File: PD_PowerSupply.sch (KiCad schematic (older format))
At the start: 75 parts, among them J1 2.54mm Header, J2 Screw Terminal, Q1 STL6P3LLH6, Q2 STL6P3LLH6, U1 LM1117LD-3.3, U2 STUSB4500QTR, U3 LMR16006YQ5, U4 LTM8074IY, U5 LTC7106EDDB-1, U6 LMP92064SDE_NOPB, U8 BMD-340-A-R, U9 USB6B1

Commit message: Fixed DRC errors, moved silkscreen
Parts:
- gave numbers to parts that had none: 1
- renumbered TP3 to LED_DATA1
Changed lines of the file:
@@
 Connection ~ 3550 4450
 $Comp
-L Connector:TestPoint TP3
+L Connector:TestPoint LED_DATA1
 U 1 1 5F110793
 P 5650 8850
-F 0 "TP3" H 5600 9100 50  0000 L CNN
+F 0 "LED_DATA1" H 5500 9050 50  0000 L CNN
 F 1 "TestPoint" H 5708 8877 50  0001 L CNN
 F 2 "TestPoint:TestPoint_Pad_D1.0mm" H 5850 8850 50  0001 C CNN
@@
 	8850 1500 12800 1500
 $Comp
-L AQV252GAX:AQV252GAX U?
+L AQV252GAX:AQV252GAX U7
 U 1 1 5F123B82
 P 17100 1950
-F 0 "U?" V 17096 1720 50  0000 R CNN
+F 0 "U7" V 17096 1720 50  0000 R CNN
 F 1 "AQV252GAX" V 17005 1720 50  0000 R CNN
 F 2 "SOP6" H 17100 1950 50  0001 L BNN

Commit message: Setup fab drawing and remove designators from silk
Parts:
- added LMP_CSB1, LTC_CSB1, LTC_EN1, MISO1, MOSI1, SCLK1: TestPoint, TestPoint:TestPoint_Pad_D1.0mm, symbol Connector:TestPoint
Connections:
- net labels added: USB_D_N, USB_D_P, USB_TVS_N, USB_TVS_P
- wire segments 362 -> 373
- no-connect marks 13 -> 14
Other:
- moved on the sheet: C15, C16, C17, C18, D3, I2C_SCL1, I2C_SDA1, L1, R20, R21, R22, U1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

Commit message: Generated gerbers, started BOM setup for PCBWay
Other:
- note added: "FIX INDUCTOR"
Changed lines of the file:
@@
 	1    0    0    -1
 $EndComp
+Text Notes 4800 11550 0    50   ~ 0
+FIX INDUCTOR
 $EndSCHEMATC

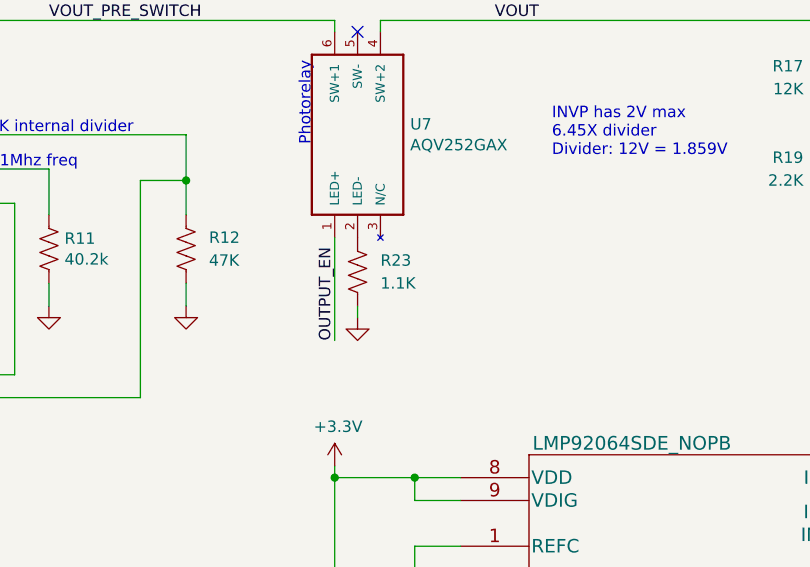
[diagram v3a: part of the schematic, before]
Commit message: Generate gerbers, drill, centroid, and BOM
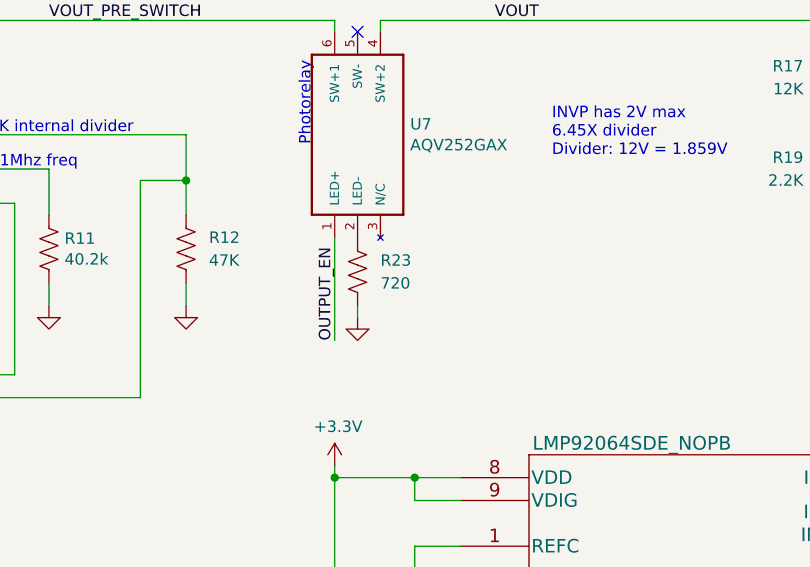
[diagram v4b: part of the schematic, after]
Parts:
- R23: value 1.1K -> 720
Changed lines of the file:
@@
 P 17100 2600
 F 0 "R23" H 17200 2650 50  0000 L CNN
-F 1 "1.1K" H 17200 2550 50  0000 L CNN
+F 1 "720" H 17200 2550 50  0000 L CNN
 F 2 "Resistor_SMD:R_0603_1608Metric" V 17140 2590 50  0001 C CNN
 F 3 "~" H 17100 2600 50  0001 C CNN

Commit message: Switched to PWM DAC
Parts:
- removed U5: LTC7106EDDB-1, ul_LTC7106EDDB:LTC7106EDDB, symbol 2020-04-18_18-56-16:LTC7106EDDB-1
- added BUCK_ENABLE1, DACOUTA1, DACOUTB1: TestPoint, TestPoint:TestPoint_Pad_D1.0mm, symbol Connector:TestPoint
- added C28: 0.1uF, Capacitor_SMD:C_0603_1608Metric, symbol Device:C
- added R24: 10k, Resistor_SMD:R_0603_1608Metric, symbol Device:R_US
- added U5: LTC2644CMS-L10#PBF, SOP65P490X110-12N_LTC2644CMS-L10#PBF, symbol LTC2644CMS-L10_PBF:LTC2644CMS-L10#PBF
- R12: value 47K -> 15k
- R15: value 10k -> DNP
- R7: value 10k -> 3.9k
- renumbered LTC_EN1 to DACPWMA1, LTC_CSB1 to DACPWMB1
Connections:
- net labels added: BUCK_ENABLE, DACPWMA, DACPWMB
- net labels removed: LTC7106_CSB, LTC7106_EN
- wire segments 373 -> 392
- no-connect marks 14 -> 13
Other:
- note added: "Temporarily using STL8P4LLF6\nOriginal PN out of stock"
- note removed: "FIX INDUCTOR"
- note removed: "Switching regulator controller\n(Current DAC)"
- note removed: "VOut accuracy: \n1.0V to 8.9V: 0.06V (nom range)\n9.0V to 12V: 0.25V (high range)"
- moved on the sheet: C10, R10, R15, R7

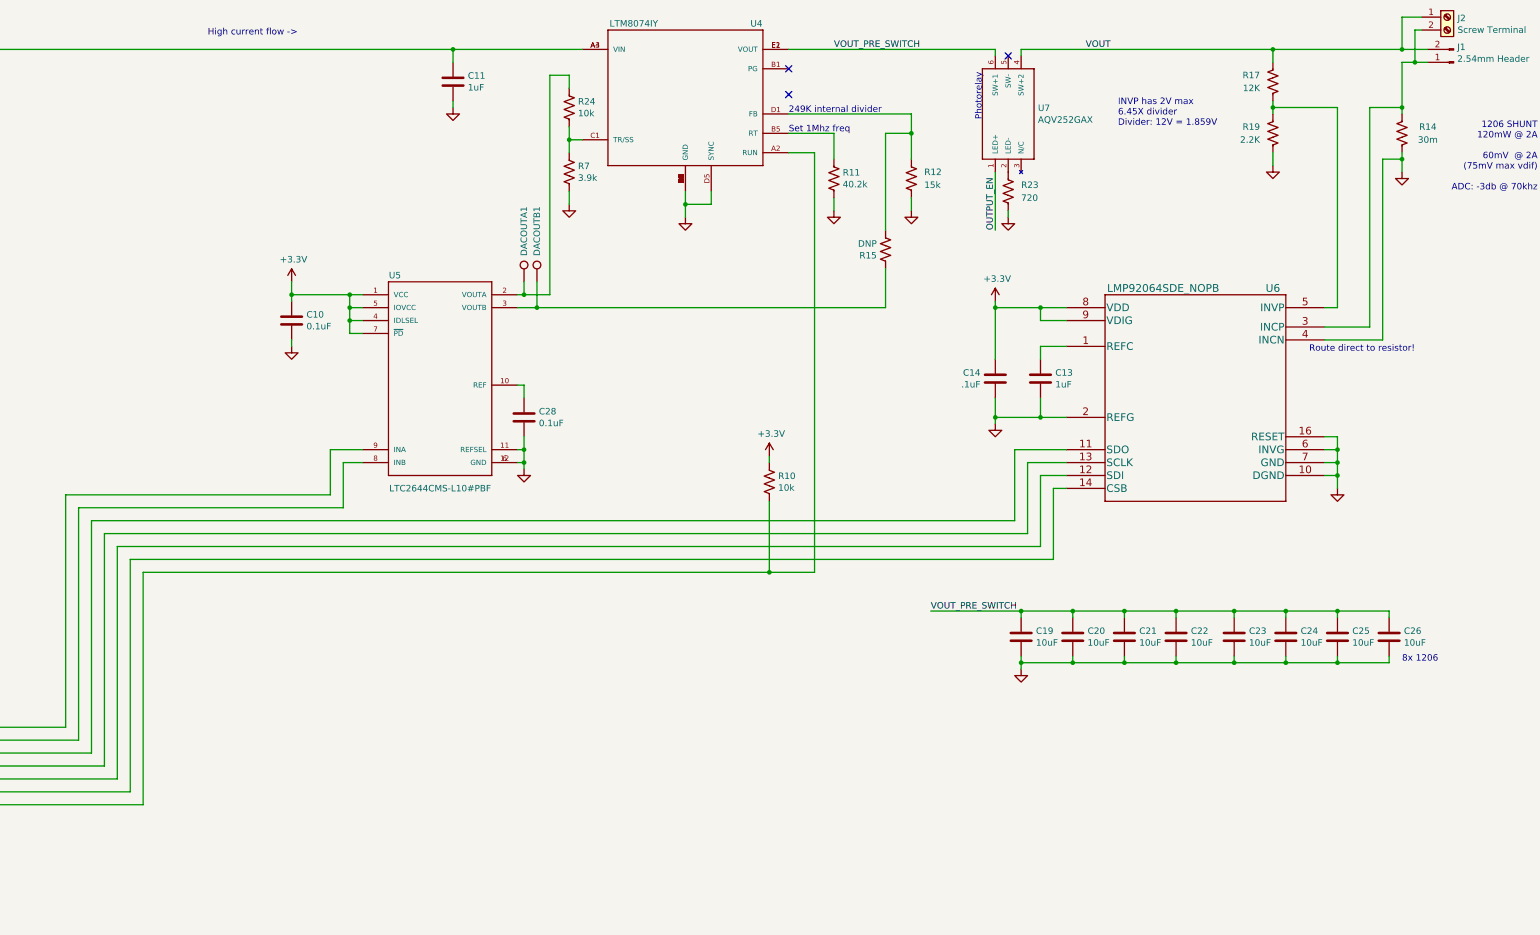
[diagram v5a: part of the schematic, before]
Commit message: Added level shifter for ADC
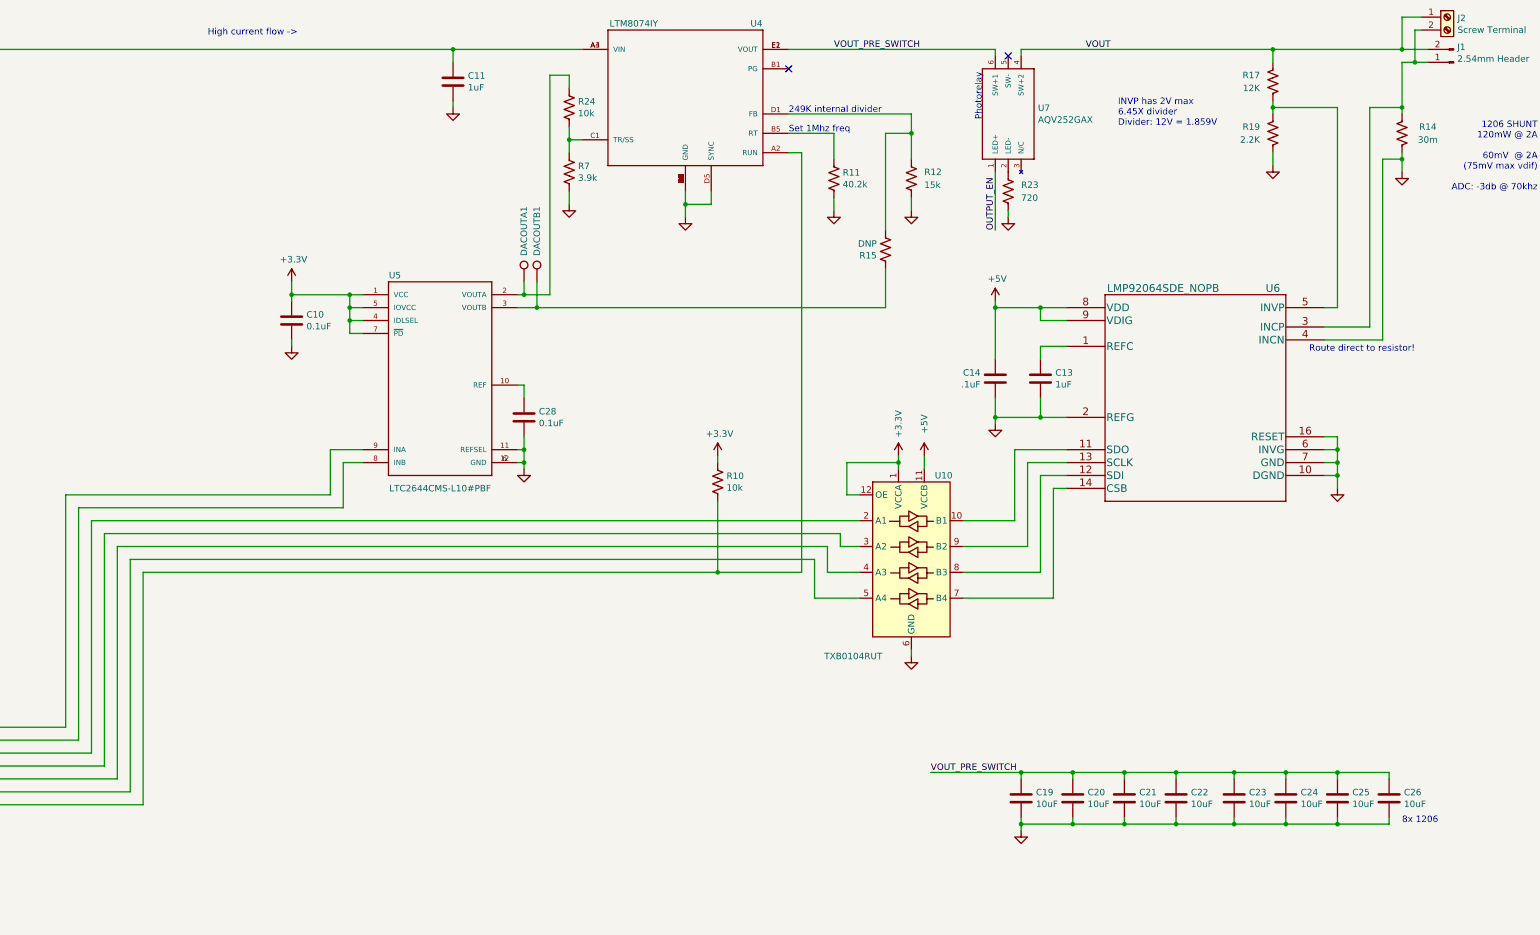
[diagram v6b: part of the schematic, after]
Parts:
- added U10: TXB0104RUT, Package_DFN_QFN:Texas_R_PUQFN-N12, symbol Logic_LevelTranslator:TXB0104RUT
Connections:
- net +3V3: now also U10.1 (VCCA), U10.12 (OE); no longer C14.1, U6.8 (VDD), U6.9 (VDIG)
- net +5V: now also C14.1, U6.8 (VDD), U6.9 (VDIG), U10.11 (VCCB)
- net GND: now also U10.6 (GND)
- net LMP92064_CSB: now also U10.5 (A4); no longer U6.14 (CSB)
- net MISO: now also U10.2 (A1); no longer U6.11 (SDO)
- net MOSI: now also U10.4 (A3); no longer U6.12 (SDI)
- net SCLK: now also U10.3 (A2); no longer U6.13 (SCLK)
- new net: U10.10 (B1), U6.11 (SDO)
- new net: U10.8 (B3), U6.12 (SDI)
- new net: U10.9 (B2), U6.13 (SCLK)
- new net: U10.7 (B4), U6.14 (CSB)
- no-connect marks 13 -> 12
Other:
- moved on the sheet: C19, C20, C21, C22, C23, C24, C25, C26, R10

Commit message: after testing, removed FB resistors and backup PWM DAC channel
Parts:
- removed DACOUTB1: TestPoint, TestPoint:TestPoint_Pad_D1.0mm, symbol Connector:TestPoint
- removed R15: DNP, Resistor_SMD:R_0603_1608Metric, symbol Device:R_US
- removed R21: 54.9K, Resistor_SMD:R_0603_1608Metric, symbol Device:R_US
- removed R22: 10K, Resistor_SMD:R_0603_1608Metric, symbol Device:R_US
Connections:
- net +5V: now also U3.3 (FB)
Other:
- note added: "Internal feedback divider for 5V"
- note added: "USB-C"
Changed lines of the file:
@@
 Title "USB PD Power Supply"
 Date "2020-03-22"
-Rev "1"
-Comp ""
+Rev "2"
+Comp "Captio Labs"
 Comment1 ""
 Comment2 ""
@@
 Wire Wire Line
 	9800 6750 6150 6750
-$Comp
-L Device:R_US R15
-U 1 1 5EAE45A7
-P 16150 3050
-F 0 "R15" H 16218 3096 50  0000 L CNN
-F 1 "DNP" H 16218 3005 50  0000 L CNN
-F 2 "Resistor_SMD:R_0603_1608Metric" V 16190 3040 50  0001 C CNN
-F 3 "~" H 16150 3050 50  0001 C CNN
-	1    16150 3050
-	-1   0    0    1
-$EndComp
 $Comp
 L 2020-05-08_21-34-57:LMP92064SDE_NOPB U6
@@
 Wire Wire Line
 	3600 12700 3600 12650
-$Comp
-L Device:R_US R21
-U 1 1 5F469F42
-P 5700 12250
-F 0 "R21" H 5768 12296 50  0000 L CNN
-F 1 "54.9K" H 5768 12205 50  0000 L CNN
-F 2 "Resistor_SMD:R_0603_1608Metric" V 5740 12240 50  0001 C CNN
-F 3 "~" H 5700 12250 50  0001 C CNN
-	1    5700 12250
-	1    0    0    -1
-$EndComp
 Wire Wire Line
 	5550 11650 5700 11650
-$Comp
-L Device:R_US R22
-U 1 1 5F46B0E3
-P 5700 12650
-F 0 "R22" H 5768 12696 50  0000 L CNN
-F 1 "10K" H 5768 12605 50  0000 L CNN
-F 2 "Resistor_SMD:R_0603_1608Metric" V 5740 12640 50  0001 C CNN
-F 3 "~" H 5700 12650 50  0001 C CNN
-	1    5700 12650
-	1    0    0    -1
-$EndComp
-Wire Wire Line
-	5700 12500 5700 12450
-$Comp
-L power:GND #PWR016
-U 1 1 5F4C1D2E
-P 5700 12850
-F 0 "#PWR016" H 5700 12600 50  0001 C CNN
-F 1 "GND" H 5700 12700 50  0001 C CNN
-F 2 "" H 5700 12850 50  0001 C CNN
-F 3 "" H 5700 12850 50  0001 C CNN
-	1    5700 12850
-	1    0    0    -1
-$EndComp
-Wire Wire Line
-	5700 12850 5700 12800
 $Comp
 L Device:C C17
@@
 Wire Wire Line
 	10300 5450 10300 7250
-Wire Wire Line
-	5700 12450 5700 12400
-Connection ~ 5700 12450
-Wire Wire Line
-	5700 11650 5700 12100
 Text Notes 15400 2000 0    50   ~ 0
 249K internal divider
@@
 Text Notes 7150 1150 0    50   ~ 0
 Temporarily using STL8P4LLF6\nOriginal PN out of stock
-Wire Wire Line
-	16350 2000 16350 2150
-Wire Wire Line
-	16150 2900 16150 2150
-Wire Wire Line
-	16150 2150 16350 2150
-Connection ~ 16350 2150
-Wire Wire Line
-	16350 2150 16350 2350
-Wire Wire Line
-	16150 3500 16150 3200
 $Comp
 L LTC2644CMS-L10_PBF:LTC2644CMS-L10#PBF U5
@@
 	9900 5050 11950 5050
 Wire Wire Line
-	13300 3500 13450 3500
-Wire Wire Line
 	13300 3400 13350 3400
 Text Label 5000 7350 0    50   ~ 0
@@
 	1    0    0    -1
 $EndComp
-$Comp
-L Connector:TestPoint DACOUTB1
-U 1 1 5F3B380F
-P 13450 3300
-F 0 "DACOUTB1" V 13450 3500 50  0000 L CNN
-F 1 "TestPoint" H 13508 3327 50  0001 L CNN
-F 2 "TestPoint:TestPoint_Pad_D1.0mm" H 13650 3300 50  0001 C CNN
-F 3 "~" H 13650 3300 50  0001 C CNN
-	1    13450 3300
-	1    0    0    -1
-$EndComp
 Wire Wire Line
 	13350 3300 13350 3400
-Wire Wire Line
-	13450 3300 13450 3500
-Connection ~ 13450 3500
-Wire Wire Line
-	13450 3500 16150 3500
 Wire Wire Line
 	9800 4950 11850 4950
@@
 Wire Wire Line
 	15500 2300 15500 5550
+Wire Wire Line
+	5700 11650 5700 12450
+Text Notes 4200 12650 0    50   ~ 0
+Internal feedback divider for 5V
+Text Notes 1600 4600 0    50   ~ 0
+USB-C
+Wire Wire Line
+	16350 2000 16350 2350
 $EndSCHEMATC

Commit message: remove feedback divider from 5V buck (internal divider)
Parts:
- U3: symbol Regulator_Switching:LMR16006YQ5 -> PD_PowerSupply-rescue:LMR16006YQ5-Regulator_Switching
- U9: symbol Power_Protection:USB6B1 -> PD_PowerSupply-rescue:USB6B1-Power_Protection
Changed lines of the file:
@@
 	20150 1500 20350 1500
 $Comp
-L Regulator_Switching:LMR16006YQ5 U3
+L PD_PowerSupply-rescue:LMR16006YQ5-Regulator_Switching U3
 U 1 1 5EA28B43
 P 3600 11700
@@
 	2100 3550 2100 3600
 $Comp
-L Power_Protection:USB6B1 U9
+L PD_PowerSupply-rescue:USB6B1-Power_Protection U9
 U 1 1 5EC72E1B
 P 2650 5250
